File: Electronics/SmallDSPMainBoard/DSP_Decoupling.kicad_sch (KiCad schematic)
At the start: 24 parts

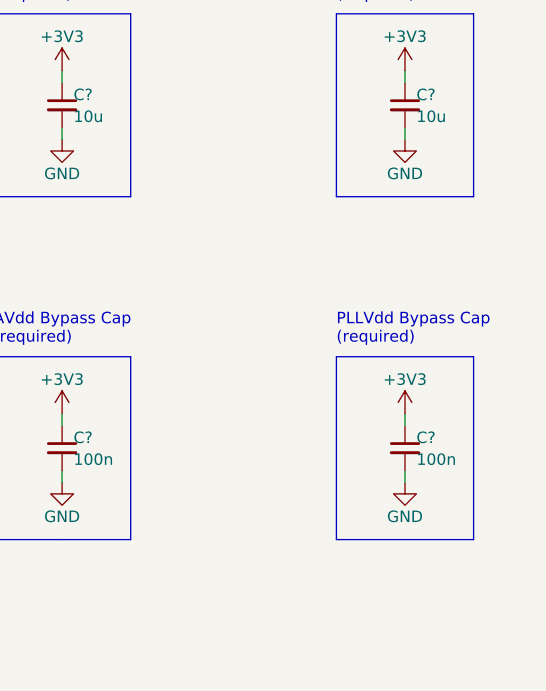
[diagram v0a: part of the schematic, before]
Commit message: Adds seperate ground for crystal and pll
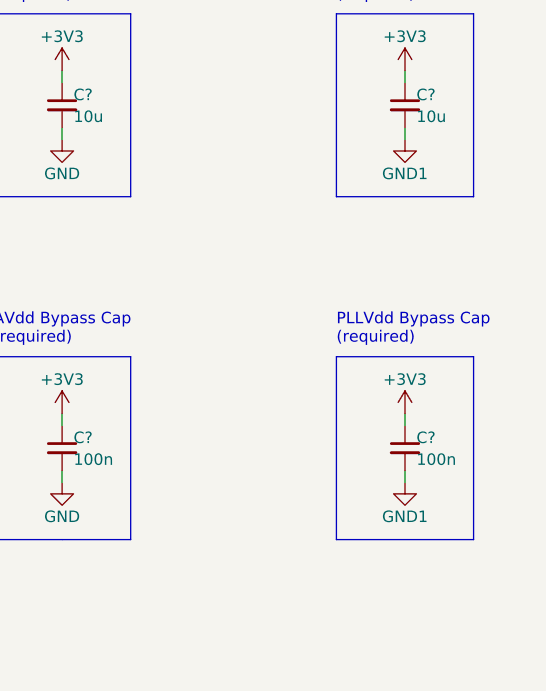
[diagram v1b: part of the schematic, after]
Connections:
- net GND: no longer C?.2, C?.2
- new net GND1: C?.2, C?.2
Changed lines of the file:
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@@
+    )
+  )
+  (symbol (lib_id "power:GND1") (at 241.3 90.17 0) (unit 1)
+    (in_bom yes) (on_board yes) (dnp no)
+    (property "Reference" "#PWR0220" (at 241.3 96.52 0)
+      (effects (font (size 1.27 1.27)) hide)
+    )
+    (property "Value" "GND1" (at 241.3 93.98 0)
+      (effects (font (size 1.27 1.27)))
+    )
+    (property "Footprint" "" (at 241.3 90.17 0)
+      (effects (font (size 1.27 1.27)) hide)
+    )
+    (property "Datasheet" "" (at 241.3 90.17 0)
+      (effects (font (size 1.27 1.27)) hide)
+    )
+    (pin "1")
+    (instances
+      (project "SmallDSPMainBoard"
+        (path "/5f2729b5-edcd-4fbc-b3fb-44096724c941"
+          (reference "#PWR0220") (unit 1)
+        )
+        (path "/5f2729b5-edcd-4fbc-b3fb-44096724c941/4d9b9490-10af-4217-8f51-0bf6380e804c"
+          (reference "#PWR0207") (unit 1)
+        )
+      )
     )
   )
@@
     )
   )
+  (symbol (lib_id "power:GND1") (at 241.3 52.07 0) (unit 1)
+    (in_bom yes) (on_board yes) (dnp no)
+    (property "Reference" "#PWR0220" (at 241.3 58.42 0)
+      (effects (font (size 1.27 1.27)) hide)
+    )
+    (property "Value" "GND1" (at 241.3 55.88 0)
+      (effects (font (size 1.27 1.27)))
+    )
+    (property "Footprint" "" (at 241.3 52.07 0)
+      (effects (font (size 1.27 1.27)) hide)
+    )
+    (property "Datasheet" "" (at 241.3 52.07 0)
+      (effects (font (size 1.27 1.27)) hide)
+    )
+    (pin "1")
+    (instances
+      (project "SmallDSPMainBoard"
+        (path "/5f2729b5-edcd-4fbc-b3fb-44096724c941"
+          (reference "#PWR0220") (unit 1)
+        )
+        (path "/5f2729b5-edcd-4fbc-b3fb-44096724c941/4d9b9490-10af-4217-8f51-0bf6380e804c"
+          (reference "#PWR0205") (unit 1)
+        )
+      )
+    )
+  )
   (symbol (lib_id "power:+1V2") (at 88.9 44.45 0) (unit 1)
     (in_bom yes) (on_board yes) (dnp no)
@@
     )
   )
-  (symbol (lib_id "power:GND") (at 241.3 90.17 0) (unit 1)
-    (in_bom yes) (on_board yes) (dnp no)
-    (property "Reference" "#PWR?" (at 241.3 96.52 0)
-      (effects (font (size 1.27 1.27)) hide)
-    )
-    (property "Value" "GND" (at 241.3 93.98 0)
-      (effects (font (size 1.27 1.27)))
-    )
-    (property "Footprint" "" (at 241.3 90.17 0)
-      (effects (font (size 1.27 1.27)) hide)
-    )
-    (property "Datasheet" "" (at 241.3 90.17 0)
-      (effects (font (size 1.27 1.27)) hide)
-    )
-    (pin "1")
-    (instances
-      (project "SmallDSPMainBoard"
-        (path "/5f2729b5-edcd-4fbc-b3fb-44096724c941"
-          (reference "#PWR?") (unit 1)
-        )
-        (path "/5f2729b5-edcd-4fbc-b3fb-44096724c941/4d9b9490-10af-4217-8f51-0bf6380e804c"
-          (reference "#PWR0207") (unit 1)
-        )
-      )
-    )
-  )
   (symbol (lib_id "power:+1V2") (at 85.09 82.55 0) (unit 1)
     (in_bom yes) (on_board yes) (dnp no)
@@
         )
       )
-    )
-  )
-  (symbol (lib_id "power:GND") (at 241.3 52.07 0) (unit 1)
-    (in_bom yes) (on_board yes) (dnp no)
-    (property "Reference" "#PWR?" (at 241.3 58.42 0)
-      (effects (font (size 1.27 1.27)) hide)
-    )
-    (property "Value" "GND" (at 241.3 55.88 0)
-      (effects (font (size 1.27 1.27)))
-    )
-    (property "Footprint" "" (at 241.3 52.07 0)
-      (effects (font (size 1.27 1.27)) hide)
-    )
-    (property "Datasheet" "" (at 241.3 52.07 0)
-      (effects (font (size 1.27 1.27)) hide)
-    )
-    (pin "1")
-    (instances
-      (project "SmallDSPMainBoard"
-        (path "/5f2729b5-edcd-4fbc-b3fb-44096724c941"
-          (reference "#PWR?") (unit 1)
-        )
-        (path "/5f2729b5-edcd-4fbc-b3fb-44096724c941/4d9b9490-10af-4217-8f51-0bf6380e804c"
-          (reference "#PWR0205") (unit 1)
-        )
-      )

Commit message: Partly finishes layout
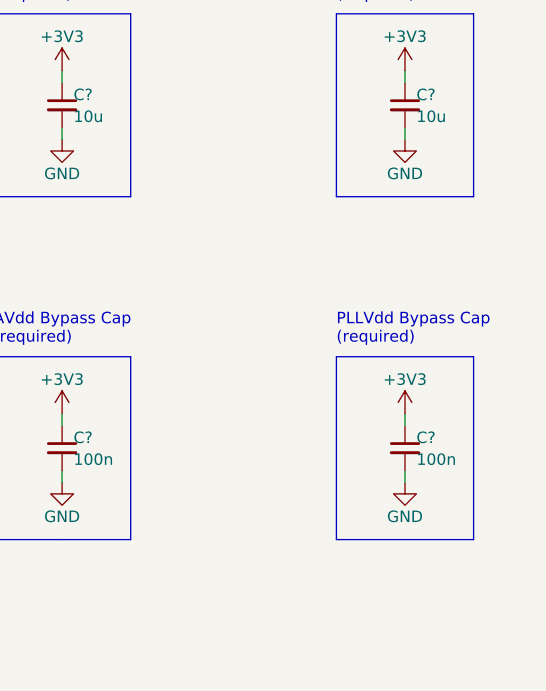
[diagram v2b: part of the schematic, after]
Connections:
- net GND1 is gone; now on net GND: C?.2, C?.2
